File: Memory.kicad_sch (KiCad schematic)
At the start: 30 parts, among them J1 Micro_SD_Card_Det, U1 IMX6UL, U5 MKDN0xxxCL, U6 MT41K256M16TW, U7 MT41K256M16TW

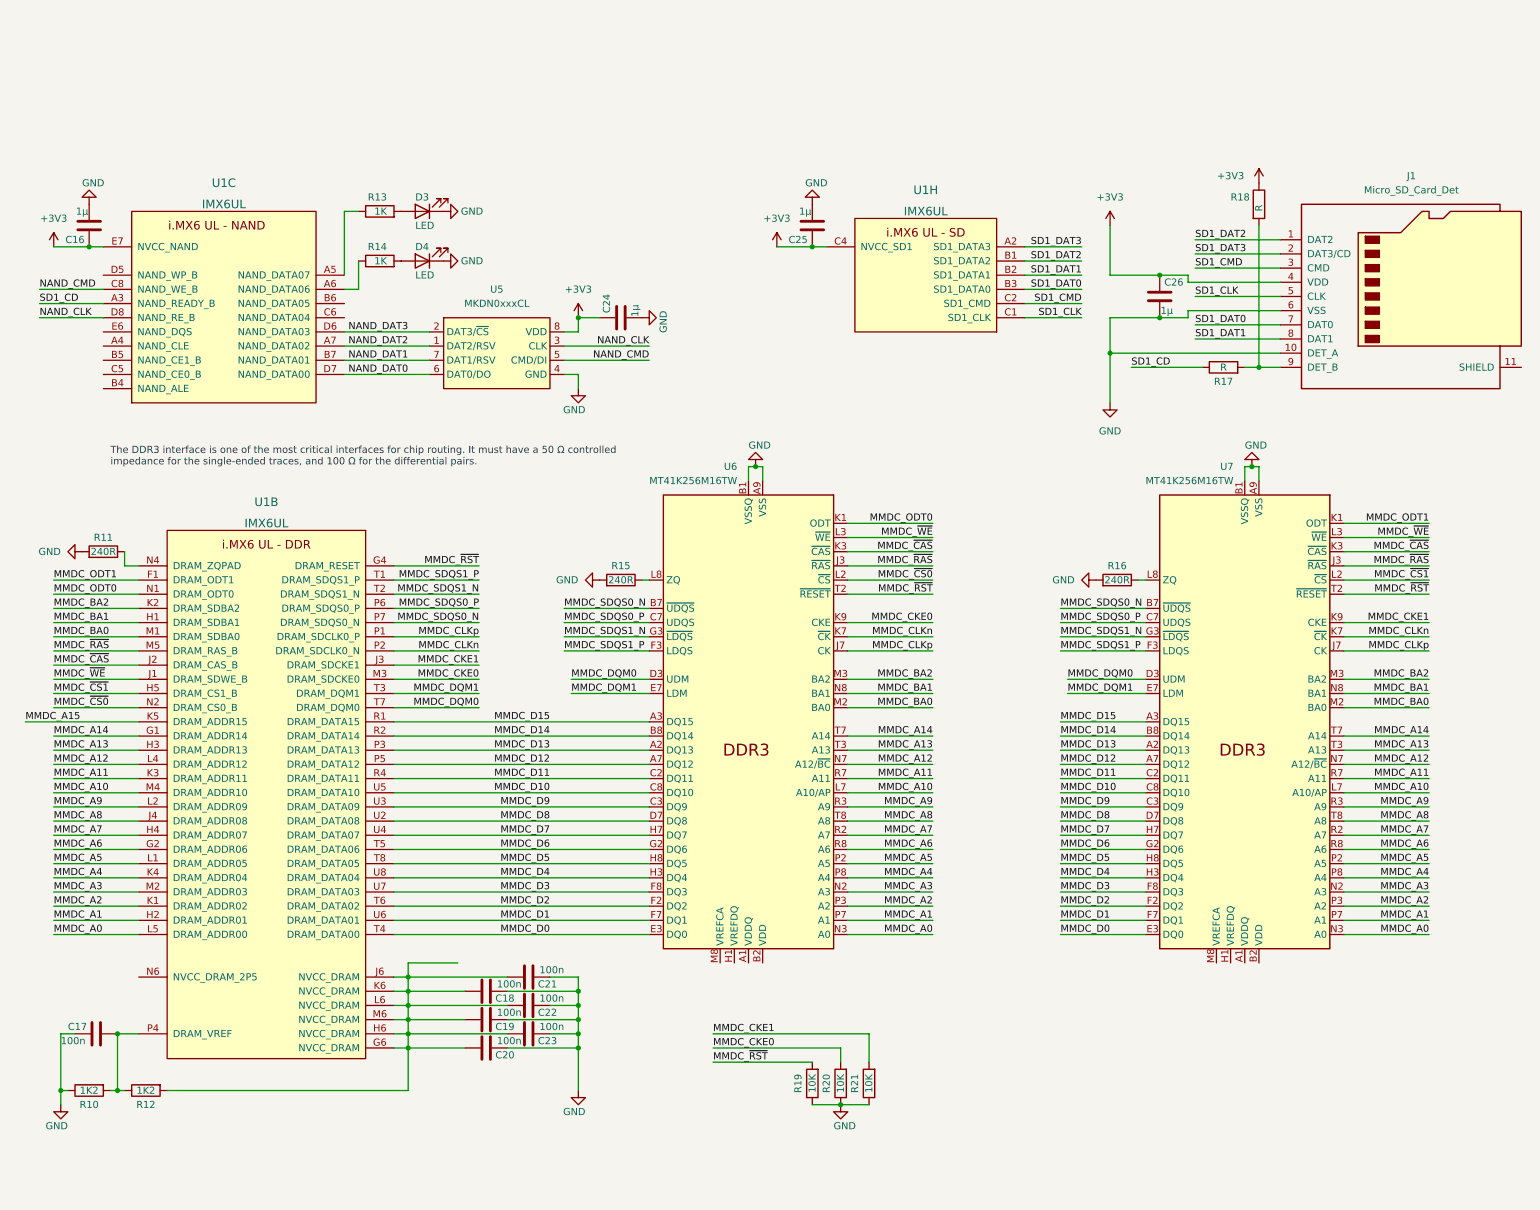
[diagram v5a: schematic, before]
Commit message: update DDR
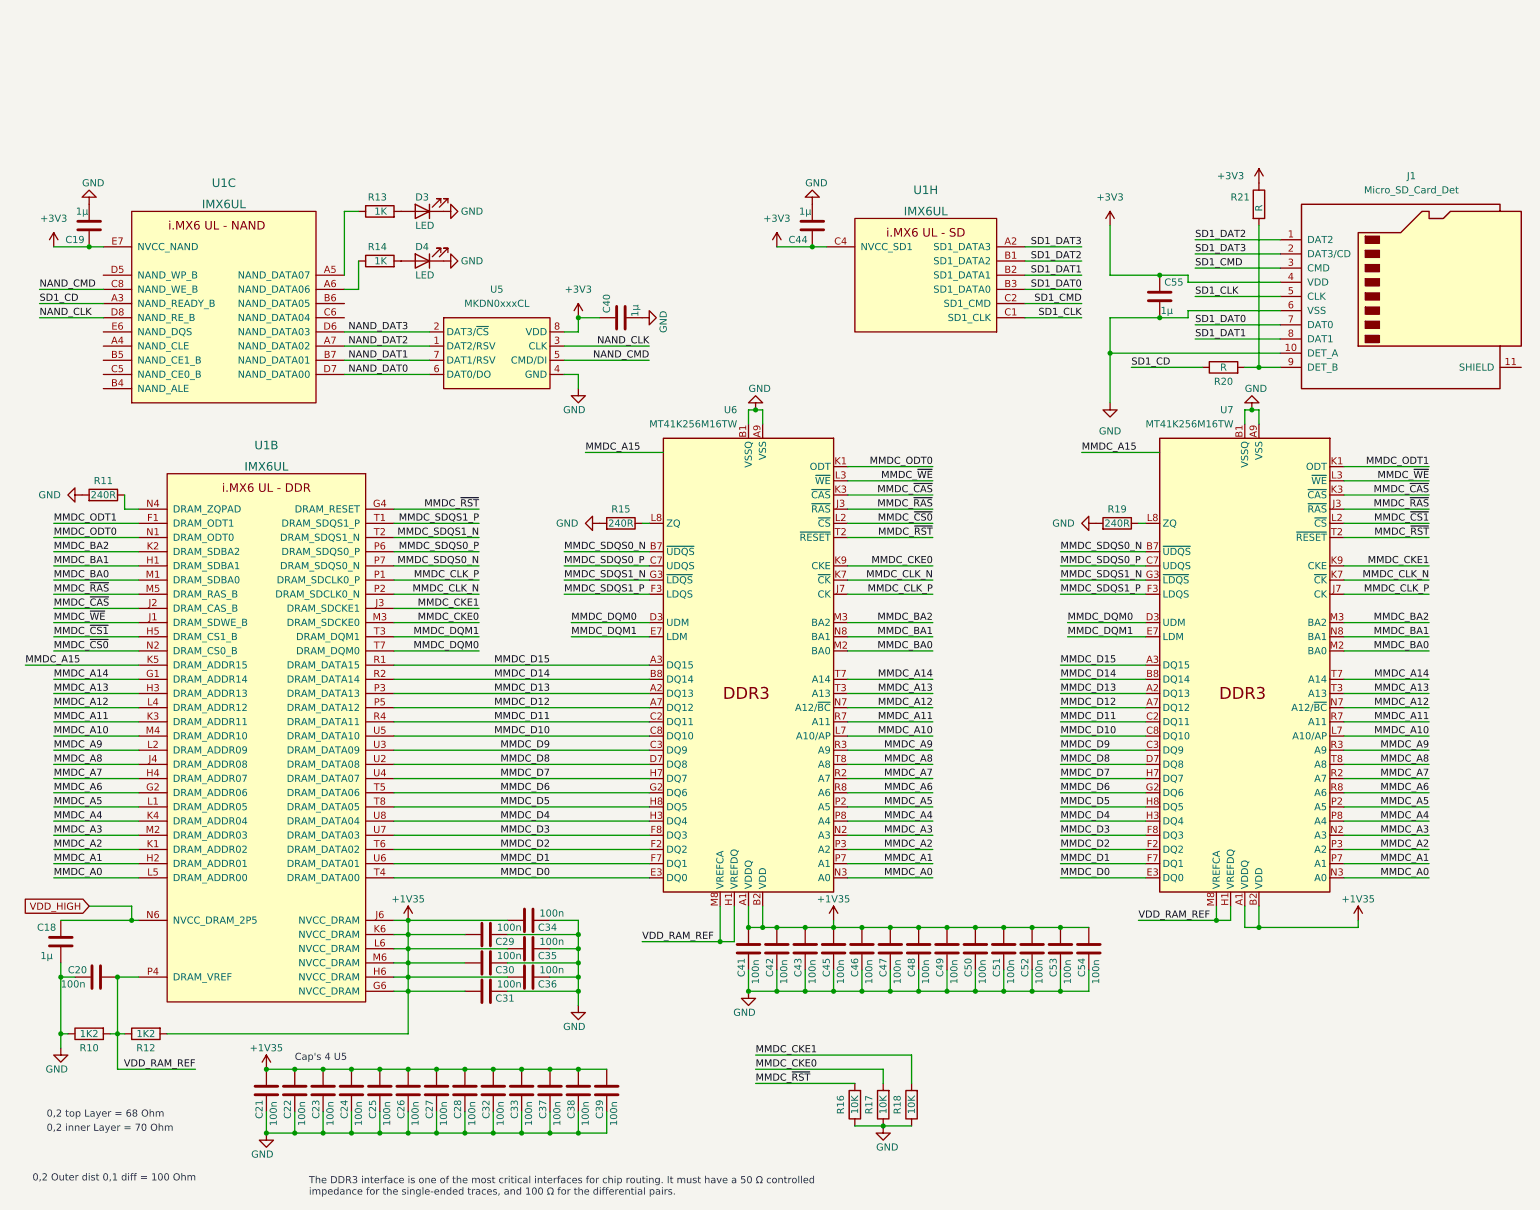
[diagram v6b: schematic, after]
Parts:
- added C18: 1µ, Capacitor_SMD:C_0402_1005Metric, symbol Device:C
- added C21, C22, C23, C24, C25, C26, C27, C28, C32, C33, C37, C38, C39, C41, C42, C43, C45, C46, C47, C48, C49, C50, C51, C52, C53, C54: 100n, Capacitor_SMD:C_0402_1005Metric, symbol Device:C
- R15: footprint (none) -> Resistor_SMD:R_0402_1005Metric
- R19: renamed from R16; footprint (none) -> Resistor_SMD:R_0402_1005Metric
- renumbered C16 to C19, C17 to C20, C18 to C29, C19 to C30, C20 to C31, C21 to C34, C22 to C35, C23 to C36, C24 to C40, C25 to C44, C26 to C55, R19 to R16, R20 to R17, R21 to R18, R17 to R20, R18 to R21
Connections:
- net GND: now also C18.1, C21.2, C22.2, C23.2, C24.2, C25.2, C26.2, C27.2, C28.2, C32.2, C33.2, C37.2, C38.2, C39.2, C41.2, C42.2, C43.2, C45.2, C46.2, C47.2, C48.2, C49.2, C50.2, C51.2, C52.2, C53.2, C54.2
- net MMDC_A15: now also U6.M7 (NC), U7.M7 (NC)
- net +1V35: now reaches C29.1, C30.1, C31.1, C34.1, C35.1, C36.1, R12.2, U1.G6 (NVCC_DRAM), U1.H6 (NVCC_DRAM), U1.J6 (NVCC_DRAM), U1.K6 (NVCC_DRAM), U1.L6 (NVCC_DRAM), U1.M6 (NVCC_DRAM)
- net +1V35: now also U6.A1 (VDDQ), U6.A8 (VDDQ), U6.B2 (VDD), U6.C1 (VDDQ), U6.C9 (VDDQ), U6.D2 (VDDQ), U6.D9 (VDD), U6.E9 (VDDQ), U6.F1 (VDDQ), U6.G7 (VDD), U6.H2 (VDDQ), U6.H9 (VDDQ), U6.K2 (VDD), U6.K8 (VDD), U6.N1 (VDD), U6.N9 (VDD), U6.R1 (VDD), U6.R9 (VDD), U7.A1 (VDDQ), U7.A8 (VDDQ), U7.B2 (VDD), U7.C1 (VDDQ), U7.C9 (VDDQ), U7.D2 (VDDQ), U7.D9 (VDD), U7.E9 (VDDQ), U7.F1 (VDDQ), U7.G7 (VDD), U7.H2 (VDDQ), U7.H9 (VDDQ), U7.K2 (VDD), U7.K8 (VDD), U7.N1 (VDD), U7.N9 (VDD), U7.R1 (VDD), U7.R9 (VDD), C21.1, C22.1, C23.1, C24.1, C25.1, C26.1, C27.1, C28.1, C32.1, C33.1, C37.1, C38.1, C39.1, C41.1, C42.1, C43.1, C45.1, C46.1, C47.1, C48.1, C49.1, C50.1, C51.1, C52.1, C53.1, C54.1
- net VDD_HIGH: now reaches U1.N6 (NVCC_DRAM_2P5)
- net VDD_HIGH: now also C18.2
- net VDD_RAM_REF: now reaches C20.1, R10.2, R12.1, U1.P4 (DRAM_VREF)
- net VDD_RAM_REF: now also U6.H1 (VREFDQ), U6.M8 (VREFCA), U7.H1 (VREFDQ), U7.M8 (VREFCA)
- net MMDC_CLKn renamed MMDC_CLK_N
- net MMDC_CLKp renamed MMDC_CLK_P
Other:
- note added: "0,2 Outer dist 0,1 diff = 100 Ohm"
- note added: "0,2 inner Layer = 70 Ohm"
- note added: "0,2 top Layer = 68 Ohm"
- note added: "Cap's 4 U5"
- moved on the sheet: C20, C29, C30, C31, C34, C35, C36, R10, R11, R12, R15, R16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
